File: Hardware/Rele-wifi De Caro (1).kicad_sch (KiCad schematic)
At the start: 38 parts, among them IC1 MC7805CD2TG, J1 Screw_Terminal_01x03, J2 Screw_Terminal_01x03, J3 Screw_Terminal_01x03, J4 Screw_Terminal_01x03, J5 Screw_Terminal_01x02, K1 PR13-5V-450-1C, K2 PR13-5V-450-1C, K3 PR13-5V-450-1C, K4 PR13-5V-450-1C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

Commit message: PCB casi terminado
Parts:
- D3, D4, D6, D8: footprint Diode_SMD:D_0805_2012Metric -> Diode_SMD:D_SMA
- SW1: footprint (none) -> Connector_PinHeader_2.54mm:PinHeader_1x02_P2.54mm_Vertical
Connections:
- net GND: now also U2.P$2 (GND)
- net GPIO 16: now reaches U2.P$15 (IO16)
- net GPIO 16: now also R4.1
- net GPIO 4: now reaches U2.P$8 (IO4)
- net GPIO 4: now also R2.1
- net GPIO 13: no longer names the net of U2.P$4 (IO13)
- net GPIO 13: no longer R2.1
- net GPIO 14: no longer names the net of U2.P$6 (IO14)
- net GPIO 14: no longer R4.1
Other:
- moved on the sheet: 10K4, D7, D8, J4, K4, Q7, Q8, R4

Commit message: Add files via upload
PCB terminado
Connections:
- net GPIO 13: now reaches U2.P$4 (IO13)
- net GPIO 13: now also R4.1
- net GPIO 14: now reaches U2.P$6 (IO14)
- net GPIO 14: now also R3.1
- net GPIO 2: now reaches U2.P$7 (IO2)
- net GPIO 2: now also R1.1
- net GPIO 12: no longer names the net of U2.P$3 (IO12)
- net GPIO 12: no longer R3.1
- net GPIO 15: no longer names the net of U2.P$5 (IO15)
- net GPIO 15: no longer R1.1
- net GPIO 16: no longer names the net of U2.P$15 (IO16)
- net GPIO 16: no longer R4.1
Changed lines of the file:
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@@
+	(wire
+		(pts
+			(xy 111.506 147.32) (xy 114.3 147.32)
+		)
+		(stroke
+			(width 0)
+			(type default)
+		)
+	)
 	(wire
 		(pts
@@
 	(wire
 		(pts
-			(xy 111.506 144.78) (xy 114.3 144.78)
-		)
-		(stroke
-			(width 0)
-			(type default)
-		)
-	)
-	(wire
-		(pts
 			(xy 226.06 29.21) (xy 226.06 30.988)
 		)
@@
 	(wire
 		(pts
+			(xy 111.506 154.94) (xy 114.3 154.94)
+		)
+		(stroke
+			(width 0)
+			(type default)
+		)
+	)
+	(wire
+		(pts
 			(xy 226.06 102.108) (xy 226.06 102.362)
 		)
@@
 	(wire
 		(pts
+			(xy 111.506 152.4) (xy 114.3 152.4)
+		)
+		(stroke
+			(width 0)
+			(type default)
+		)
+	)
+	(wire
+		(pts
 			(xy 187.96 39.37) (xy 187.96 39.878)
 		)
@@
 	(wire
 		(pts
-			(xy 147.32 142.24) (xy 144.78 142.24)
-		)
-		(stroke
-			(width 0)
-			(type default)
-		)
-	)
-	(wire
-		(pts
 			(xy 91.44 102.108) (xy 91.44 102.362)
 		)
@@
 		(pts
 			(xy 91.44 29.21) (xy 91.44 30.988)
-		)
-		(stroke
-			(width 0)
-			(type default)
-		)
-	)
-	(wire
-		(pts
-			(xy 111.506 149.86) (xy 114.3 149.86)
 		)
 		(stroke
@@
 		)
 	)
-	(global_label "GPIO 16"
+	(global_label "GPIO 13"
 		(shape input)
 		(at 34.29 78.74 180)
@@
 		)
 	)
-	(global_label "GPIO 15"
+	(global_label "GPIO 2"
 		(shape input)
-		(at 111.506 149.86 180)
+		(at 111.506 154.94 180)
 		(fields_autoplaced yes)
 		(effects
@@
 		)
 		(property "Intersheetrefs" "${INTERSHEET_REFS}"
-			(at 100.6589 149.86 0)
+			(at 101.8684 154.94 0)
 			(effects
 				(font
@@
 		)
 	)
-	(global_label "GPIO 16"
+	(global_label "GPIO 13"
 		(shape input)
-		(at 147.32 142.24 0)
+		(at 111.506 147.32 180)
 		(fields_autoplaced yes)
 		(effects
@@
 				(size 1.27 1.27)
 			)
-			(justify left)
+			(justify right)
 		)
 		(property "Intersheetrefs" "${INTERSHEET_REFS}"
-			(at 158.1671 142.24 0)
-			(effects
-				(font
-					(size 1.27 1.27)
-				)
-				(justify left)
-				(hide yes)
-			)
-		)
-	)
-	(global_label "GPIO 12"
-		(shape input)
-		(at 111.506 144.78 180)
-		(fields_autoplaced yes)
-		(effects
-			(font
-				(size 1.27 1.27)
-			)
-			(justify right)
-		)
-		(property "Intersheetrefs" "${INTERSHEET_REFS}"
-			(at 100.6589 144.78 0)
+			(at 100.6589 147.32 0)
 			(effects
 				(font
@@
 		)
 	)
-	(global_label "GPIO 15"
+	(global_label "GPIO 14"
+		(shape input)
+		(at 111.506 152.4 180)
+		(fields_autoplaced yes)
+		(effects
+			(font
+				(size 1.27 1.27)
+			)
+			(justify right)
+		)
+		(property "Intersheetrefs" "${INTERSHEET_REFS}"
+			(at 100.6589 152.4 0)
+			(effects
+				(font
+					(size 1.27 1.27)
+				)
+				(justify right)
+				(hide yes)
+			)
+		)
+	)
+	(global_label "GPIO 2"
 		(shape input)
 		(at 168.91 78.74 180)
@@
 		)
 		(property "Intersheetrefs" "${INTERSHEET_REFS}"
-			(at 158.0629 78.74 0)
+			(at 159.2724 78.74 0)
 			(effects
 				(font
@@
 		)
 	)
-	(global_label "GPIO 12"
+	(global_label "GPIO 14"
 		(shape input)
 		(at 34.29 29.21 180)

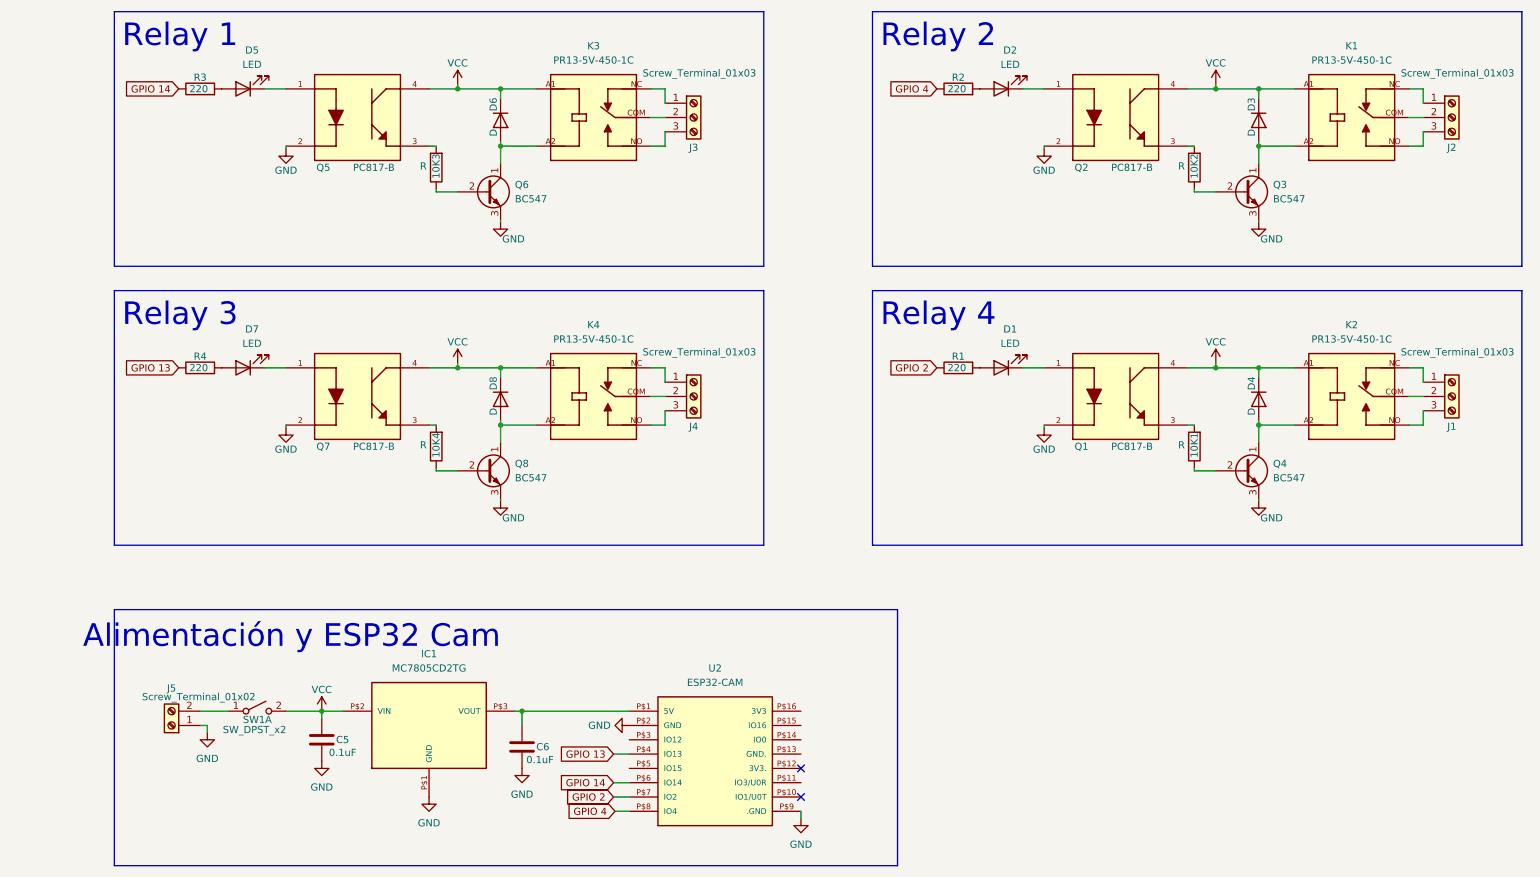
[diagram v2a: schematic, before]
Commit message: PCB terminado y prolijo
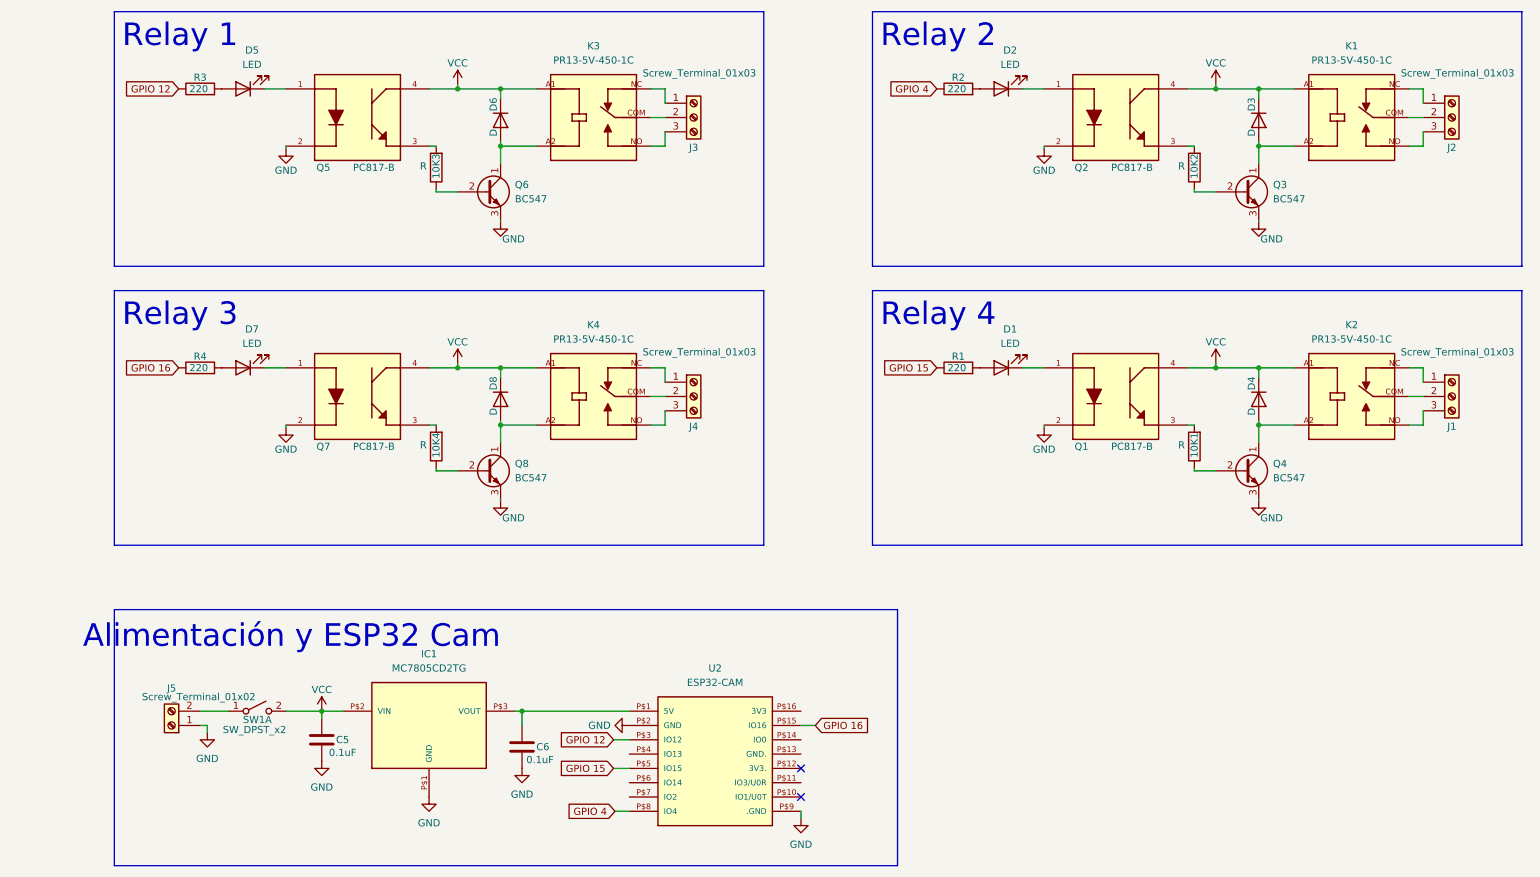
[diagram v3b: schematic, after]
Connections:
- net GPIO 16: now reaches U2.P$15 (IO16)
- net GPIO 16: now also R4.1
- net GPIO 12: now reaches U2.P$3 (IO12)
- net GPIO 12: now also R3.1
- net GPIO 15: now reaches U2.P$5 (IO15)
- net GPIO 15: now also R1.1
- net GPIO 13: no longer names the net of U2.P$4 (IO13)
- net GPIO 13: no longer R4.1
- net GPIO 14: no longer names the net of U2.P$6 (IO14)
- net GPIO 14: no longer R3.1
- net GPIO 2: no longer names the net of U2.P$7 (IO2)
- net GPIO 2: no longer R1.1
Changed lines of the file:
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@@
-	(wire
-		(pts
-			(xy 111.506 147.32) (xy 114.3 147.32)
-		)
-		(stroke
-			(width 0)
-			(type default)
-		)
-	)
 	(wire
 		(pts
@@
 	(wire
 		(pts
+			(xy 111.506 144.78) (xy 114.3 144.78)
+		)
+		(stroke
+			(width 0)
+			(type default)
+		)
+	)
+	(wire
+		(pts
 			(xy 226.06 29.21) (xy 226.06 30.988)
 		)
@@
 	(wire
 		(pts
-			(xy 111.506 154.94) (xy 114.3 154.94)
-		)
-		(stroke
-			(width 0)
-			(type default)
-		)
-	)
-	(wire
-		(pts
 			(xy 226.06 102.108) (xy 226.06 102.362)
 		)
@@
 	(wire
 		(pts
-			(xy 111.506 152.4) (xy 114.3 152.4)
-		)
-		(stroke
-			(width 0)
-			(type default)
-		)
-	)
-	(wire
-		(pts
 			(xy 187.96 39.37) (xy 187.96 39.878)
 		)
@@
 	(wire
 		(pts
+			(xy 147.32 142.24) (xy 144.78 142.24)
+		)
+		(stroke
+			(width 0)
+			(type default)
+		)
+	)
+	(wire
+		(pts
 			(xy 91.44 102.108) (xy 91.44 102.362)
 		)
@@
 		(pts
 			(xy 91.44 29.21) (xy 91.44 30.988)
+		)
+		(stroke
+			(width 0)
+			(type default)
+		)
+	)
+	(wire
+		(pts
+			(xy 111.506 149.86) (xy 114.3 149.86)
 		)
 		(stroke
@@
 		)
 	)
-	(global_label "GPIO 13"
+	(global_label "GPIO 16"
 		(shape input)
 		(at 34.29 78.74 180)
@@
 		)
 	)
-	(global_label "GPIO 2"
+	(global_label "GPIO 15"
 		(shape input)
-		(at 111.506 154.94 180)
+		(at 111.506 149.86 180)
 		(fields_autoplaced yes)
 		(effects
@@
 		)
 		(property "Intersheetrefs" "${INTERSHEET_REFS}"
-			(at 101.8684 154.94 0)
+			(at 100.6589 149.86 0)
 			(effects
 				(font
@@
 		)
 	)
-	(global_label "GPIO 13"
+	(global_label "GPIO 16"
 		(shape input)
-		(at 111.506 147.32 180)
+		(at 147.32 142.24 0)
 		(fields_autoplaced yes)
 		(effects
@@
 				(size 1.27 1.27)
 			)
+			(justify left)
+		)
+		(property "Intersheetrefs" "${INTERSHEET_REFS}"
+			(at 158.1671 142.24 0)
+			(effects
+				(font
+					(size 1.27 1.27)
+				)
+				(justify left)
+				(hide yes)
+			)
+		)
+	)
+	(global_label "GPIO 12"
+		(shape input)
+		(at 111.506 144.78 180)
+		(fields_autoplaced yes)
+		(effects
+			(font
+				(size 1.27 1.27)
+			)
 			(justify right)
 		)
 		(property "Intersheetrefs" "${INTERSHEET_REFS}"
-			(at 100.6589 147.32 0)
+			(at 100.6589 144.78 0)
 			(effects
 				(font
@@
 		)
 	)
-	(global_label "GPIO 14"
-		(shape input)
-		(at 111.506 152.4 180)
-		(fields_autoplaced yes)
-		(effects
-			(font
-				(size 1.27 1.27)
-			)
-			(justify right)
-		)
-		(property "Intersheetrefs" "${INTERSHEET_REFS}"
-			(at 100.6589 152.4 0)
-			(effects
-				(font
-					(size 1.27 1.27)
-				)
-				(justify right)
-				(hide yes)
-			)
-		)
-	)
-	(global_label "GPIO 2"
+	(global_label "GPIO 15"
 		(shape input)
 		(at 168.91 78.74 180)
@@
 		)
 		(property "Intersheetrefs" "${INTERSHEET_REFS}"
-			(at 159.2724 78.74 0)
+			(at 158.0629 78.74 0)
 			(effects
 				(font
@@
 		)
 	)
-	(global_label "GPIO 14"
+	(global_label "GPIO 12"
 		(shape input)
 		(at 34.29 29.21 180)

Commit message: PCB terminado 2.0
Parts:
- removed Q3, Q4, Q6, Q8: BC547, bc547 smd:SOT95P230X110-3N, symbol EESTN5:BC547
- added Q10, Q11, Q12, Q9: BC847, Package_TO_SOT_SMD:SOT-23, symbol Transistor_BJT:BC847
- added R5, R6, R7, R8: 680, Resistor_SMD:R_0805_2012Metric_Pad1.20x1.40mm_HandSolder, symbol Device:R
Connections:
- net GND: now also Q10.2 (E), Q11.2 (E), Q12.2 (E), Q9.2 (E)
- net GPIO 16: now also U2.P$4 (IO13); no longer U2.P$15 (IO16)
- net VCC: now also R5.2, R6.2, R7.2, R8.2
- net at D3.2 (A), K1.A2: now also D2.1 (K), Q12.3 (C)
- net at Q1.1: now also R1.2; no longer D1.1 (K)
- net at 10K1.1: now also Q11.1 (B)
- net at R4.2: now also Q7.1; no longer D7.2 (A)
- net at 10K2.1: now also Q12.1 (B)
- net at D7.1 (K): now also D8.2 (A), K4.A2, Q10.3 (C); no longer Q7.1
- net at D5.2 (A): now also R8.1; no longer R3.2
- net at Q5.1: now also R3.2; no longer D5.1 (K)
- net at D6.2 (A), K3.A2: now also D5.1 (K), Q9.3 (C)
- net at D4.2 (A), K2.A2: now also D1.1 (K), Q11.3 (C)
- net at 10K4.1: now also Q10.1 (B)
- net at R2.2: now also Q2.1; no longer D2.2 (A)
- net at 10K3.1: now also Q9.1 (B)
- net at D1.2 (A): now also R5.1; no longer R1.2
- new net: D7.2 (A), R7.1
- new net: D2.2 (A), R6.1
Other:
- moved on the sheet: D1, D2, D5, D7, R1, R3, R4
